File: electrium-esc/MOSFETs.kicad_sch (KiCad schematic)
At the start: 12 parts

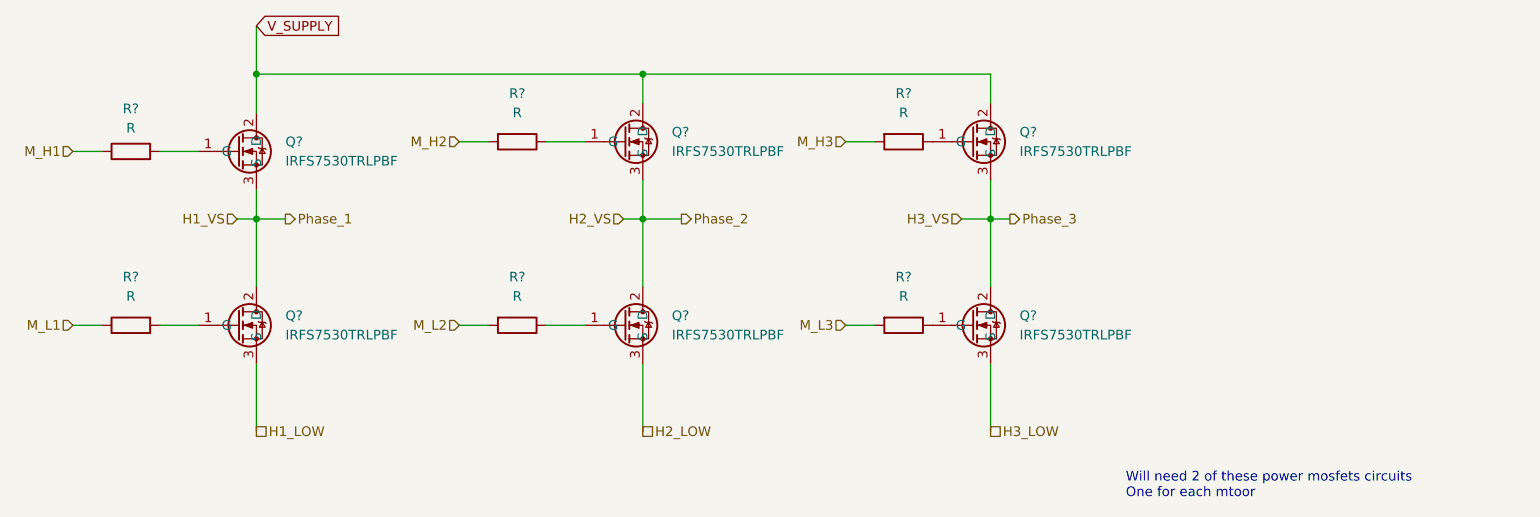
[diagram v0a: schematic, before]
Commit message: Update MOSFETs.kicad_sch
updated schematic with resistor values
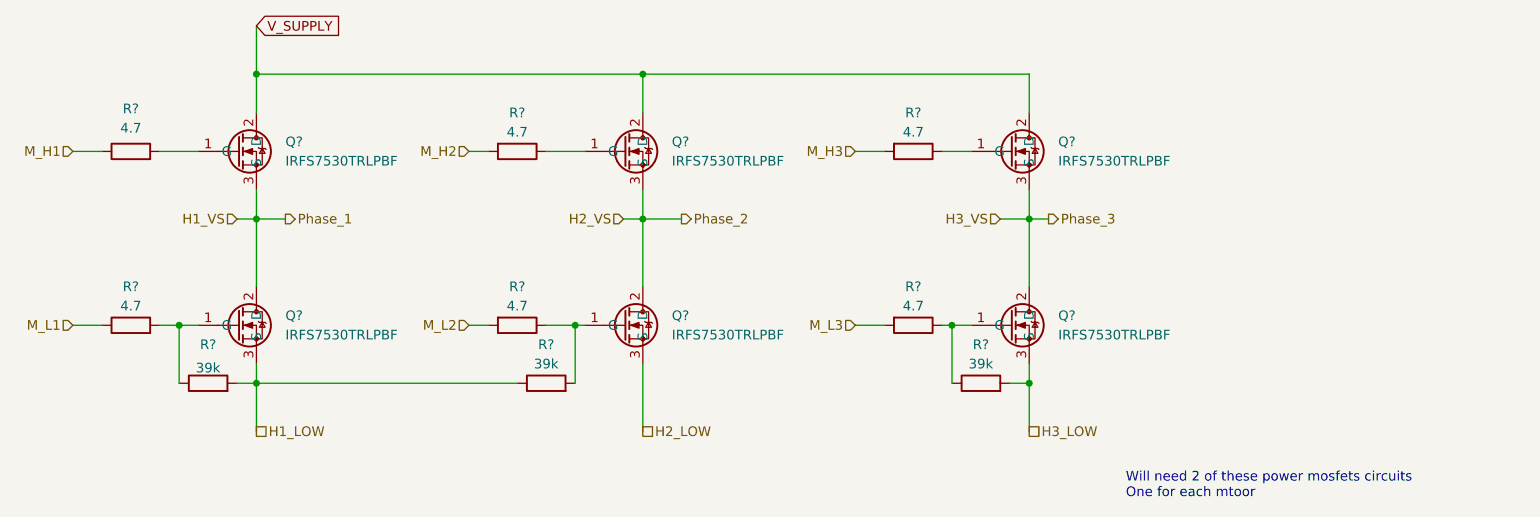
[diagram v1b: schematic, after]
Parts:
- added R? (x3): 39k, symbol Device:R
- R? (x6): value R -> 4.7
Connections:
- net H1_LOW: now also R?.1, R?.2
- net H3_LOW: now also R?.2
- net at Q?.1 (G), R?.2: now also R?.1
- net at Q?.1 (G), R?.1: now also R?.2
- net at Q?.1 (G), R?.1: now also R?.1
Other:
- moved on the sheet: Q?, R?

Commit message: Prototype (almost) finished
Have to do electric check rules
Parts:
- R? (x6): value 4.7 -> 4R7
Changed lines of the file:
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@@
     (data
       iVBORw0KGgoAAAANSUhEUgAAAW8AAAEFCAIAAACjMfF/AAAAA3NCSVQICAjb4U/gAAAACXBIWXMA
-      AA7DAAAOwwHHb6hkAAAgAElEQVR4nOy9d3hU15k/fu6904v6qCAhRBEgIZAAYwhgOgFTjLHBdrC9
+      AA50AAAOdAFrJLPWAAAgAElEQVR4nOy9d3hU15k/fu6904v6qCAhRBEgIZAAYwhgOgFTjLHBdrC9
       bkncEifZbJLN+ll/Y2dj7z7PZtdxHCcuxAbj4DiGuMgEY7rpYBCiI4F6L6Myvdz7++Oz9/0dRkgg
       MdLIeD5/8IyGO3fO3HPOe97yed9XUBSFRRFFFFHcMMRIDyCKKKK4SRCVJlFEEUV4EJUmUUQRRXgQ
@@
     (effects (font (size 1.27 1.27)) (justify left))
   )
-  (hierarchical_label "H2_VS" (shape input) (at 151.13 81.28 180)
+  (hierarchical_label "H2_VS" (shape output) (at 151.13 81.28 180)
     (effects (font (size 1.27 1.27)) (justify right))
   )
-  (hierarchical_label "H1_VS" (shape input) (at 100.33 81.28 180)
+  (hierarchical_label "H1_VS" (shape output) (at 100.33 81.28 180)
     (effects (font (size 1.27 1.27)) (justify right))
   )
@@
     (effects (font (size 1.27 1.27)) (justify right))
   )
-  (hierarchical_label "H3_VS" (shape input) (at 200.66 81.28 180)
+  (hierarchical_label "H3_VS" (shape output) (at 200.66 81.28 180)
     (effects (font (size 1.27 1.27)) (justify right))
   )
@@
     (in_bom yes) (on_board yes)
     (property "Reference" "R?" (id 0) (at 86.36 90.17 90))
-    (property "Value" "4.7" (id 1) (at 86.36 92.71 90))
+    (property "Value" "4R7" (id 1) (at 86.36 92.71 90))
     (property "Footprint" "" (id 2) (at 86.36 97.028 90)
       (effects (font (size 1.27 1.27)) hide)
@@
     (in_bom yes) (on_board yes)
     (property "Reference" "R?" (id 0) (at 189.23 90.17 90))
-    (property "Value" "4.7" (id 1) (at 189.23 92.71 90))
+    (property "Value" "4R7" (id 1) (at 189.23 92.71 90))
     (property "Footprint" "" (id 2) (at 189.23 93.472 90)
       (effects (font (size 1.27 1.27)) hide)
@@
     (in_bom yes) (on_board yes)
     (property "Reference" "R?" (id 0) (at 137.16 67.31 90))
-    (property "Value" "4.7" (id 1) (at 137.16 69.85 90))
+    (property "Value" "4R7" (id 1) (at 137.16 69.85 90))
     (property "Footprint" "" (id 2) (at 137.16 70.612 90)
       (effects (font (size 1.27 1.27)) hide)
@@
     (in_bom yes) (on_board yes)
     (property "Reference" "R?" (id 0) (at 189.23 67.31 90))
-    (property "Value" "4.7" (id 1) (at 189.23 69.85 90))
+    (property "Value" "4R7" (id 1) (at 189.23 69.85 90))
     (property "Footprint" "" (id 2) (at 189.23 70.612 90)
       (effects (font (size 1.27 1.27)) hide)
@@
     (in_bom yes) (on_board yes)
     (property "Reference" "R?" (id 0) (at 137.16 90.17 90))
-    (property "Value" "4.7" (id 1) (at 137.16 92.71 90))
+    (property "Value" "4R7" (id 1) (at 137.16 92.71 90))
     (property "Footprint" "" (id 2) (at 137.16 93.472 90)
       (effects (font (size 1.27 1.27)) hide)
@@
   (symbol (lib_id "Device:R") (at 86.36 72.39 90) (unit 1)
     (in_bom yes) (on_board yes) (fields_autoplaced)
-    (property "Reference" "R?" (id 0) (at 86.36 66.04 90)
-      (effects (font (size 1.27 1.27)) (justify bottom))
-    )
-    (property "Value" "4.7" (id 1) (at 86.36 68.58 90)
-      (effects (font (size 1.27 1.27)) (justify bottom))
-    )
+    (property "Reference" "R?" (id 0) (at 86.36 66.04 90))
+    (property "Value" "4R7" (id 1) (at 86.36 68.58 90))
     (property "Footprint" "" (id 2) (at 86.36 74.168 90)
       (effects (font (size 1.27 1.27)) hide)

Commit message: Fix Error
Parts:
- R32, R33, R34, R35, R36, R37, R38, R39, R40: renamed from R?; footprint (none) -> Resistor_SMD:R_0603_1608Metric
- gave numbers to parts that had none: 6
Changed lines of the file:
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@@
   (symbol (lib_id "Device:R") (at 86.36 95.25 90) (unit 1)
     (in_bom yes) (on_board yes)
-    (property "Reference" "R?" (id 0) (at 86.36 90.17 90))
+    (property "Reference" "R33" (id 0) (at 86.36 90.17 90))
     (property "Value" "4R7" (id 1) (at 86.36 92.71 90))
-    (property "Footprint" "" (id 2) (at 86.36 97.028 90)
+    (property "Footprint" "Resistor_SMD:R_0603_1608Metric" (id 2) (at 86.36 97.028 90)
       (effects (font (size 1.27 1.27)) hide)
     )
@@
   (symbol (lib_id "Transistor_FET:STB15N80K5") (at 151.13 95.25 0) (unit 1)
     (in_bom yes) (on_board yes) (fields_autoplaced)
-    (property "Reference" "Q?" (id 0) (at 157.48 93.9799 0)
+    (property "Reference" "Q4" (id 0) (at 157.48 93.9799 0)
       (effects (font (size 1.27 1.27)) (justify left))
     )
@@
   (symbol (lib_id "Device:R") (at 96.52 102.87 90) (unit 1)
     (in_bom yes) (on_board yes)
-    (property "Reference" "R?" (id 0) (at 96.52 97.79 90))
+    (property "Reference" "R34" (id 0) (at 96.52 97.79 90))
     (property "Value" "39k" (id 1) (at 96.52 101.6 90)
       (effects (font (size 1.27 1.27)) (justify top))
     )
-    (property "Footprint" "" (id 2) (at 96.52 104.648 90)
+    (property "Footprint" "Resistor_SMD:R_0603_1608Metric" (id 2) (at 96.52 104.648 90)
       (effects (font (size 1.27 1.27)) hide)
     )
@@
   (symbol (lib_id "Transistor_FET:STB15N80K5") (at 151.13 72.39 0) (unit 1)
     (in_bom yes) (on_board yes) (fields_autoplaced)
-    (property "Reference" "Q?" (id 0) (at 157.48 71.1199 0)
+    (property "Reference" "Q3" (id 0) (at 157.48 71.1199 0)
       (effects (font (size 1.27 1.27)) (justify left))
     )
@@
   (symbol (lib_id "Device:R") (at 140.97 102.87 90) (unit 1)
     (in_bom yes) (on_board yes)
-    (property "Reference" "R?" (id 0) (at 140.97 97.79 90))
+    (property "Reference" "R37" (id 0) (at 140.97 97.79 90))
     (property "Value" "39k" (id 1) (at 140.97 100.33 90))
-    (property "Footprint" "" (id 2) (at 140.97 104.648 90)
+    (property "Footprint" "Resistor_SMD:R_0603_1608Metric" (id 2) (at 140.97 104.648 90)
       (effects (font (size 1.27 1.27)) hide)
     )
@@
   (symbol (lib_id "Device:R") (at 189.23 95.25 270) (unit 1)
     (in_bom yes) (on_board yes)
-    (property "Reference" "R?" (id 0) (at 189.23 90.17 90))
+    (property "Reference" "R39" (id 0) (at 189.23 90.17 90))
     (property "Value" "4R7" (id 1) (at 189.23 92.71 90))
-    (property "Footprint" "" (id 2) (at 189.23 93.472 90)
+    (property "Footprint" "Resistor_SMD:R_0603_1608Metric" (id 2) (at 189.23 93.472 90)
       (effects (font (size 1.27 1.27)) hide)
     )
@@
   (symbol (lib_id "Device:R") (at 137.16 72.39 270) (unit 1)
     (in_bom yes) (on_board yes)
-    (property "Reference" "R?" (id 0) (at 137.16 67.31 90))
+    (property "Reference" "R35" (id 0) (at 137.16 67.31 90))
     (property "Value" "4R7" (id 1) (at 137.16 69.85 90))
-    (property "Footprint" "" (id 2) (at 137.16 70.612 90)
+    (property "Footprint" "Resistor_SMD:R_0603_1608Metric" (id 2) (at 137.16 70.612 90)
       (effects (font (size 1.27 1.27)) hide)
     )
@@
   (symbol (lib_id "Device:R") (at 189.23 72.39 270) (unit 1)
     (in_bom yes) (on_board yes)
-    (property "Reference" "R?" (id 0) (at 189.23 67.31 90))
+    (property "Reference" "R38" (id 0) (at 189.23 67.31 90))
     (property "Value" "4R7" (id 1) (at 189.23 69.85 90))
-    (property "Footprint" "" (id 2) (at 189.23 70.612 90)
+    (property "Footprint" "Resistor_SMD:R_0603_1608Metric" (id 2) (at 189.23 70.612 90)
       (effects (font (size 1.27 1.27)) hide)
     )
@@
   (symbol (lib_id "Device:R") (at 137.16 95.25 270) (unit 1)
     (in_bom yes) (on_board yes)
-    (property "Reference" "R?" (id 0) (at 137.16 90.17 90))
+    (property "Reference" "R36" (id 0) (at 137.16 90.17 90))
     (property "Value" "4R7" (id 1) (at 137.16 92.71 90))
-    (property "Footprint" "" (id 2) (at 137.16 93.472 90)
+    (property "Footprint" "Resistor_SMD:R_0603_1608Metric" (id 2) (at 137.16 93.472 90)
       (effects (font (size 1.27 1.27)) hide)
     )
@@
   (symbol (lib_id "Device:R") (at 86.36 72.39 90) (unit 1)
     (in_bom yes) (on_board yes) (fields_autoplaced)
-    (property "Reference" "R?" (id 0) (at 86.36 66.04 90))
+    (property "Reference" "R32" (id 0) (at 86.36 66.04 90))
     (property "Value" "4R7" (id 1) (at 86.36 68.58 90))
-    (property "Footprint" "" (id 2) (at 86.36 74.168 90)
+    (property "Footprint" "Resistor_SMD:R_0603_1608Metric" (id 2) (at 86.36 74.168 90)
       (effects (font (size 1.27 1.27)) hide)
     )
@@
   (symbol (lib_id "Transistor_FET:STB15N80K5") (at 201.93 72.39 0) (unit 1)
     (in_bom yes) (on_board yes) (fields_autoplaced)
-    (property "Reference" "Q?" (id 0) (at 208.28 71.1199 0)
+    (property "Reference" "Q5" (id 0) (at 208.28 71.1199 0)
       (effects (font (size 1.27 1.27)) (justify left))
     )
@@
   (symbol (lib_id "Transistor_FET:STB15N80K5") (at 201.93 95.25 0) (unit 1)
     (in_bom yes) (on_board yes) (fields_autoplaced)
-    (property "Reference" "Q?" (id 0) (at 208.28 93.9799 0)
+    (property "Reference" "Q6" (id 0) (at 208.28 93.9799 0)
       (effects (font (size 1.27 1.27)) (justify left))
     )
@@
   (symbol (lib_id "Transistor_FET:STB15N80K5") (at 100.33 72.39 0) (unit 1)
     (in_bom yes) (on_board yes) (fields_autoplaced)
-    (property "Reference" "Q?" (id 0) (at 106.68 71.1199 0)
+    (property "Reference" "Q1" (id 0) (at 106.68 71.1199 0)
       (effects (font (size 1.27 1.27)) (justify left))
     )
@@
   (symbol (lib_id "Device:R") (at 198.12 102.87 90) (unit 1)
     (in_bom yes) (on_board yes)
-    (property "Reference" "R?" (id 0) (at 198.12 97.79 90))
+    (property "Reference" "R40" (id 0) (at 198.12 97.79 90))
     (property "Value" "39k" (id 1) (at 198.12 100.33 90))
-    (property "Footprint" "" (id 2) (at 198.12 104.648 90)
+    (property "Footprint" "Resistor_SMD:R_0603_1608Metric" (id 2) (at 198.12 104.648 90)
       (effects (font (size 1.27 1.27)) hide)
     )
@@
   (symbol (lib_id "Transistor_FET:STB15N80K5") (at 100.33 95.25 0) (unit 1)
     (in_bom yes) (on_board yes)
-    (property "Reference" "Q?" (id 0) (at 106.68 93.9799 0)
-      (effects (font (size 1.27 1.27)) (justify left))
-    )
+    (property "Reference" "Q2" (id 0) (at 106.68 93.9799 0)
+      (effects (font (size 1.27 1.27)) (justify left))
+    )

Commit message: relabel components to make more sense
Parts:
- renumbered Q3 to Q2, Q5 to Q3, Q2 to Q4, Q4 to Q5, R32 to R34, R38 to R36, R33 to R37, R36 to R38, R34 to R40, R37 to R41, R40 to R42
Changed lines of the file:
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@@
   (symbol (lib_id "Device:R") (at 86.36 95.25 90) (unit 1)
     (in_bom yes) (on_board yes)
-    (property "Reference" "R33" (id 0) (at 86.36 90.17 90))
+    (property "Reference" "R37" (id 0) (at 86.36 90.17 90))
     (property "Value" "4R7" (id 1) (at 86.36 92.71 90))
     (property "Footprint" "Resistor_SMD:R_0603_1608Metric" (id 2) (at 86.36 97.028 90)
@@
   (symbol (lib_id "Transistor_FET:STB15N80K5") (at 151.13 95.25 0) (unit 1)
     (in_bom yes) (on_board yes) (fields_autoplaced)
-    (property "Reference" "Q4" (id 0) (at 157.48 93.9799 0)
+    (property "Reference" "Q5" (id 0) (at 157.48 93.9799 0)
       (effects (font (size 1.27 1.27)) (justify left))
     )
@@
   (symbol (lib_id "Device:R") (at 96.52 102.87 90) (unit 1)
     (in_bom yes) (on_board yes)
-    (property "Reference" "R34" (id 0) (at 96.52 97.79 90))
+    (property "Reference" "R40" (id 0) (at 96.52 97.79 90))
     (property "Value" "39k" (id 1) (at 96.52 101.6 90)
       (effects (font (size 1.27 1.27)) (justify top))
@@
   (symbol (lib_id "Transistor_FET:STB15N80K5") (at 151.13 72.39 0) (unit 1)
     (in_bom yes) (on_board yes) (fields_autoplaced)
-    (property "Reference" "Q3" (id 0) (at 157.48 71.1199 0)
+    (property "Reference" "Q2" (id 0) (at 157.48 71.1199 0)
       (effects (font (size 1.27 1.27)) (justify left))
     )
@@
   (symbol (lib_id "Device:R") (at 140.97 102.87 90) (unit 1)
     (in_bom yes) (on_board yes)
-    (property "Reference" "R37" (id 0) (at 140.97 97.79 90))
+    (property "Reference" "R41" (id 0) (at 140.97 97.79 90))
     (property "Value" "39k" (id 1) (at 140.97 100.33 90))
     (property "Footprint" "Resistor_SMD:R_0603_1608Metric" (id 2) (at 140.97 104.648 90)
@@
   (symbol (lib_id "Device:R") (at 189.23 72.39 270) (unit 1)
     (in_bom yes) (on_board yes)
-    (property "Reference" "R38" (id 0) (at 189.23 67.31 90))
+    (property "Reference" "R36" (id 0) (at 189.23 67.31 90))
     (property "Value" "4R7" (id 1) (at 189.23 69.85 90))
     (property "Footprint" "Resistor_SMD:R_0603_1608Metric" (id 2) (at 189.23 70.612 90)
@@
   (symbol (lib_id "Device:R") (at 137.16 95.25 270) (unit 1)
     (in_bom yes) (on_board yes)
-    (property "Reference" "R36" (id 0) (at 137.16 90.17 90))
+    (property "Reference" "R38" (id 0) (at 137.16 90.17 90))
     (property "Value" "4R7" (id 1) (at 137.16 92.71 90))
     (property "Footprint" "Resistor_SMD:R_0603_1608Metric" (id 2) (at 137.16 93.472 90)
@@
   (symbol (lib_id "Device:R") (at 86.36 72.39 90) (unit 1)
     (in_bom yes) (on_board yes) (fields_autoplaced)
-    (property "Reference" "R32" (id 0) (at 86.36 66.04 90))
+    (property "Reference" "R34" (id 0) (at 86.36 66.04 90))
     (property "Value" "4R7" (id 1) (at 86.36 68.58 90))
     (property "Footprint" "Resistor_SMD:R_0603_1608Metric" (id 2) (at 86.36 74.168 90)
@@
   (symbol (lib_id "Transistor_FET:STB15N80K5") (at 201.93 72.39 0) (unit 1)
     (in_bom yes) (on_board yes) (fields_autoplaced)
-    (property "Reference" "Q5" (id 0) (at 208.28 71.1199 0)
+    (property "Reference" "Q3" (id 0) (at 208.28 71.1199 0)
       (effects (font (size 1.27 1.27)) (justify left))
     )
@@
   (symbol (lib_id "Device:R") (at 198.12 102.87 90) (unit 1)
     (in_bom yes) (on_board yes)
-    (property "Reference" "R40" (id 0) (at 198.12 97.79 90))
+    (property "Reference" "R42" (id 0) (at 198.12 97.79 90))
     (property "Value" "39k" (id 1) (at 198.12 100.33 90))
     (property "Footprint" "Resistor_SMD:R_0603_1608Metric" (id 2) (at 198.12 104.648 90)
@@
   (symbol (lib_id "Transistor_FET:STB15N80K5") (at 100.33 95.25 0) (unit 1)
     (in_bom yes) (on_board yes)
-    (property "Reference" "Q2" (id 0) (at 106.68 93.9799 0)
-      (effects (font (size 1.27 1.27)) (justify left))
-    )
+    (property "Reference" "Q4" (id 0) (at 106.68 93.9799 0)
+      (effects (font (size 1.27 1.27)) (justify left))
+    )

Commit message: Change to cheaper mosfets
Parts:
- removed Q1, Q2, Q3, Q4, Q5, Q6: IRFS7530TRLPBF, Package_TO_SOT_SMD:TO-263-2, symbol Transistor_FET:STB15N80K5
- added Q1, Q2, Q3, Q4, Q5, Q6: IRF3205, Package_TO_SOT_THT:TO-220-3_Vertical, symbol Transistor_FET:IRF3205
- R34, R35, R36, R37, R38, R39, R40, R41, R42: footprint Resistor_SMD:R_0603_1608Metric -> Resistor_SMD:R_0805_2012Metric
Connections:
- net H1_LOW: now also Q4.3 (S)
- net H1_VS: now also Q1.3 (S), Q4.2 (D)
- net H2_LOW: now also Q5.3 (S)
- net H2_VS: now also Q2.3 (S), Q5.2 (D)
- net H3_LOW: now also Q6.3 (S)
- net H3_VS: now also Q3.3 (S), Q6.2 (D)
- net V_SUPPLY: now also Q1.2 (D), Q2.2 (D), Q3.2 (D)
- net at R37.2, R40.1: now also Q4.1 (G)
- net at R38.1, R41.2: now also Q5.1 (G)
- net at R35.1: now also Q2.1 (G)
- net at R39.1, R42.1: now also Q6.1 (G)
- net at R36.1: now also Q3.1 (G)
- net at R34.2: now also Q1.1 (G)
